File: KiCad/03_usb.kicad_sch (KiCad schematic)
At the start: 18 parts, among them IC301 CP2102N-A02-GQFN28R, J200 USB_C_Receptacle_USB2.0, J301 USB_C_Receptacle_USB2.0, U301 USBLC6-2SC6, U302 USBLC6-2SC6

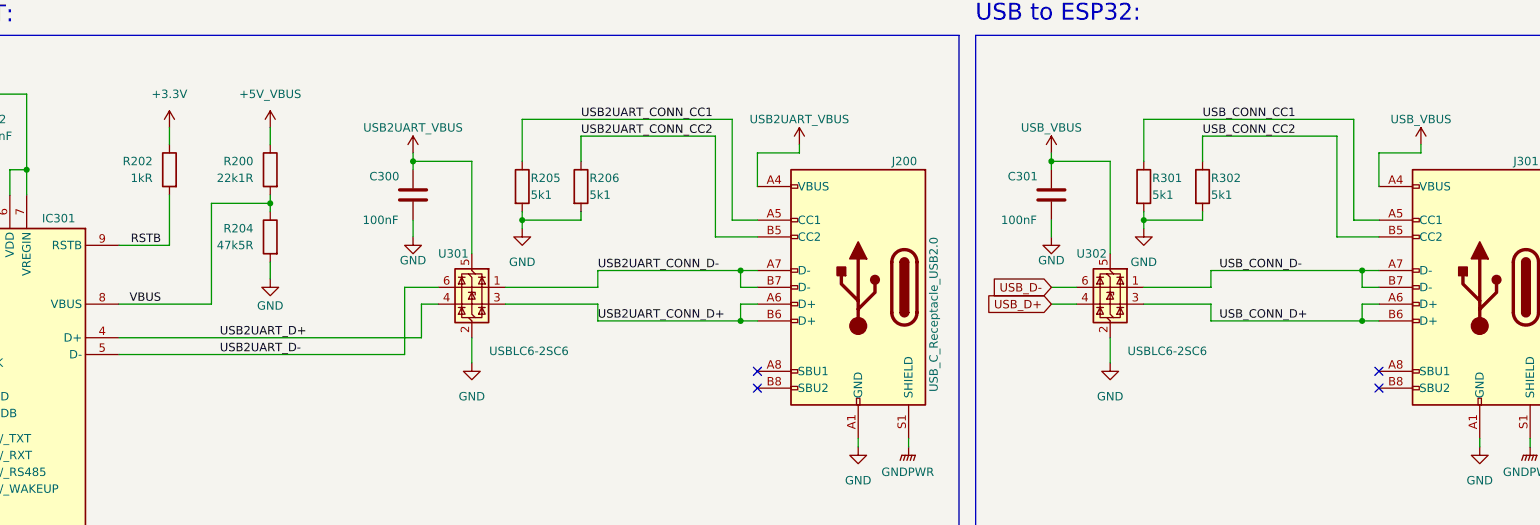
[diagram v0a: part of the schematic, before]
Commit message: Add DS3231
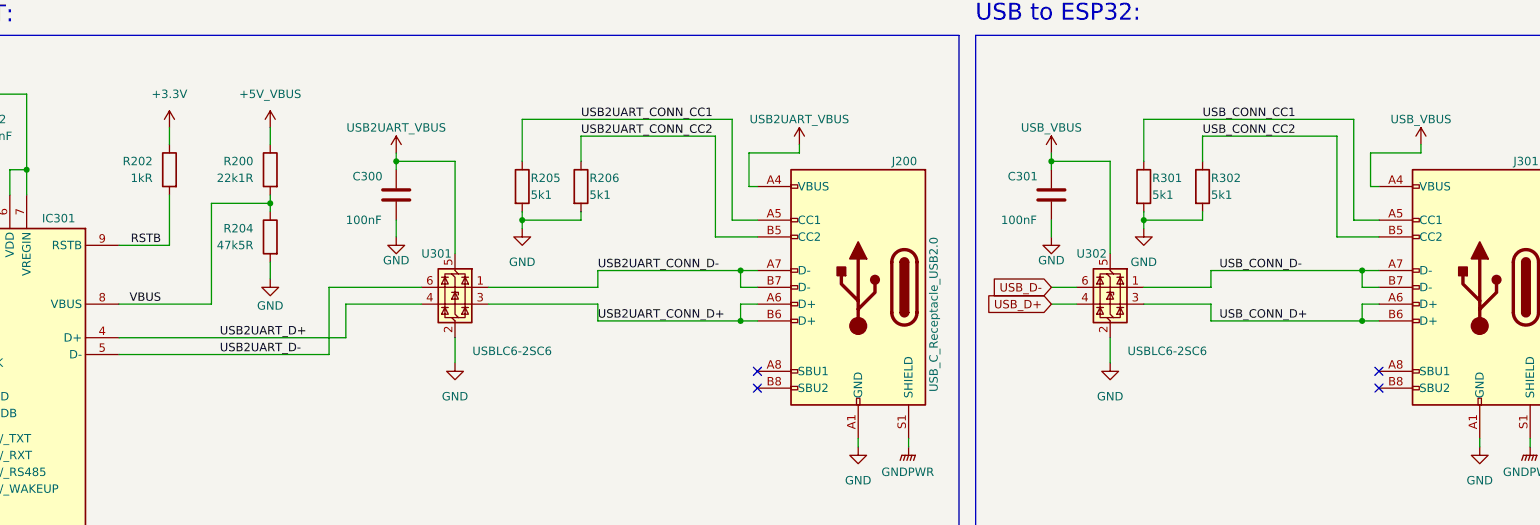
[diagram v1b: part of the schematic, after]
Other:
- moved on the sheet: C300, U301
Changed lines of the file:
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@@
 	)
 	(junction
-		(at 104.14 50.8)
+		(at 101.6 50.8)
 		(diameter 0)
 		(color 0 0 0 0)
@@
 	(wire
 		(pts
-			(xy 113.03 64.77) (xy 113.03 50.8)
+			(xy 110.49 64.77) (xy 110.49 50.8)
 		)
 		(stroke
@@
 	(wire
 		(pts
-			(xy 156.21 49.53) (xy 156.21 54.61)
+			(xy 154.94 49.53) (xy 154.94 54.61)
 		)
 		(stroke
@@
 	(wire
 		(pts
-			(xy 104.14 62.23) (xy 104.14 59.69)
+			(xy 101.6 62.23) (xy 101.6 59.69)
 		)
 		(stroke
@@
 	(wire
 		(pts
-			(xy 104.14 50.8) (xy 104.14 52.07)
+			(xy 101.6 50.8) (xy 101.6 52.07)
 		)
 		(stroke
@@
 	(wire
 		(pts
-			(xy 105.41 77.47) (xy 105.41 72.39)
+			(xy 93.98 77.47) (xy 93.98 72.39)
 		)
 		(stroke
@@
 	(wire
 		(pts
-			(xy 118.11 69.85) (xy 132.08 69.85)
+			(xy 115.57 69.85) (xy 132.08 69.85)
 		)
 		(stroke
@@
 	(wire
 		(pts
-			(xy 59.69 80.01) (xy 102.87 80.01)
+			(xy 59.69 80.01) (xy 91.44 80.01)
 		)
 		(stroke
@@
 	(wire
 		(pts
-			(xy 59.69 77.47) (xy 105.41 77.47)
+			(xy 59.69 77.47) (xy 93.98 77.47)
 		)
 		(stroke
@@
 	(wire
 		(pts
-			(xy 113.03 77.47) (xy 113.03 81.28)
+			(xy 110.49 77.47) (xy 110.49 81.28)
 		)
 		(stroke
@@
 	(wire
 		(pts
-			(xy 162.56 49.53) (xy 156.21 49.53)
+			(xy 162.56 49.53) (xy 154.94 49.53)
 		)
 		(stroke
@@
 	(wire
 		(pts
-			(xy 118.11 72.39) (xy 132.08 72.39)
+			(xy 115.57 72.39) (xy 132.08 72.39)
 		)
 		(stroke
@@
 	(wire
 		(pts
+			(xy 154.94 54.61) (xy 156.21 54.61)
+		)
+		(stroke
+			(width 0)
+			(type default)
+		)
+	)
+	(wire
+		(pts
 			(xy 224.79 72.39) (xy 224.79 74.93)
 		)
@@
 	(wire
 		(pts
-			(xy 105.41 72.39) (xy 107.95 72.39)
+			(xy 93.98 72.39) (xy 105.41 72.39)
 		)
 		(stroke
@@
 	(wire
 		(pts
-			(xy 102.87 69.85) (xy 107.95 69.85)
+			(xy 91.44 69.85) (xy 105.41 69.85)
 		)
 		(stroke
@@
 	(wire
 		(pts
-			(xy 250.19 49.53) (xy 250.19 54.61)
+			(xy 248.92 49.53) (xy 248.92 54.61)
 		)
 		(stroke
@@
 	(wire
 		(pts
-			(xy 104.14 49.53) (xy 104.14 50.8)
+			(xy 101.6 49.53) (xy 101.6 50.8)
 		)
 		(stroke
@@
 	(wire
 		(pts
+			(xy 248.92 54.61) (xy 250.19 54.61)
+		)
+		(stroke
+			(width 0)
+			(type default)
+		)
+	)
+	(wire
+		(pts
 			(xy 21.59 50.8) (xy 34.29 50.8)
 		)
@@
 	(wire
 		(pts
-			(xy 113.03 50.8) (xy 104.14 50.8)
+			(xy 110.49 50.8) (xy 101.6 50.8)
 		)
 		(stroke
@@
 	(wire
 		(pts
-			(xy 102.87 80.01) (xy 102.87 69.85)
+			(xy 91.44 80.01) (xy 91.44 69.85)
 		)
 		(stroke
@@
 	(wire
 		(pts
-			(xy 256.54 49.53) (xy 250.19 49.53)
+			(xy 256.54 49.53) (xy 248.92 49.53)
 		)
 		(stroke
@@
 	(symbol
 		(lib_id "power:VBUS")
-		(at 104.14 49.53 0)
+		(at 101.6 49.53 0)
 		(unit 1)
 		(exclude_from_sim no)
@@
 		(dnp no)
 		(property "Reference" "#PWR0311"
-			(at 104.14 53.34 0)
+			(at 101.6 53.34 0)
 			(effects
 				(font
@@
 		)
 		(property "Value" "USB2UART_VBUS"
-			(at 104.14 45.72 0)
+			(at 101.6 45.72 0)
 			(effects
 				(font
@@
 		)
 		(property "Footprint" ""
-			(at 104.14 49.53 0)
+			(at 101.6 49.53 0)
 			(effects
 				(font
@@
 		)
 		(property "Datasheet" ""
-			(at 104.14 49.53 0)
+			(at 101.6 49.53 0)
 			(effects
 				(font
@@
 		)
 		(property "Description" ""
-			(at 104.14 49.53 0)
+			(at 101.6 49.53 0)
 			(effects
 				(font
@@
 	(symbol
 		(lib_id "power:GND")
-		(at 104.14 62.23 0)
+		(at 101.6 62.23 0)
 		(mirror y)
 		(unit 1)
@@
 		(dnp no)
 		(property "Reference" "#PWR0310"
-			(at 104.14 68.58 0)
+			(at 101.6 68.58 0)
 			(effects
 				(font
@@
 		)
 		(property "Value" "GND"
-			(at 104.14 65.786 0)
+			(at 101.6 65.786 0)
 			(effects
 				(font
@@
 		)
 		(property "Footprint" ""
-			(at 104.14 62.23 0)
+			(at 101.6 62.23 0)
 			(effects
 				(font
@@
 		)
 		(property "Datasheet" ""
-			(at 104.14 62.23 0)
+			(at 101.6 62.23 0)
 			(effects
 				(font
@@
 		)
 		(property "Description" "Power symbol creates a global label with name \"GND\" , ground"
-			(at 104.14 62.23 0)
+			(at 101.6 62.23 0)
 			(effects
 				(font
@@
 	(symbol
 		(lib_id "Power_Protection:USBLC6-2SC6")
-		(at 113.03 69.85 0)
+		(at 110.49 69.85 0)
 		(mirror y)
 		(unit 1)
@@
 		(dnp no)
 		(property "Reference" "U301"
-			(at 110.236 64.77 0)
+			(at 107.696 64.77 0)
 			(effects
 				(font
@@
 		)
 		(property "Value" "USBLC6-2SC6"
-			(at 121.666 79.502 0)
+			(at 119.126 79.502 0)
 			(effects
 				(font
@@
 		)
 		(property "Footprint" "Package_TO_SOT_SMD:SOT-23-6"
-			(at 113.03 82.55 0)
+			(at 110.49 82.55 0)
 			(effects
 				(font
@@
 		)
 		(property "Datasheet" "https://www.st.com/resource/en/datasheet/usblc6-2.pdf"
-			(at 107.95 60.96 0)
+			(at 105.41 60.96 0)
 			(effects
 				(font
@@
 		)
 		(property "Description" ""
-			(at 113.03 69.85 0)
+			(at 110.49 69.85 0)
 			(effects
 				(font
@@
 		)
 		(property "Manufacturer" "STMicroelectronics"
-			(at 113.03 69.85 0)
+			(at 110.49 69.85 0)
 			(effects
 				(font
@@
 		)
 		(property "DigiKey Part Number" "497-5235-6-ND"
-			(at 113.03 69.85 0)
+			(at 110.49 69.85 0)
 			(effects
 				(font
@@
 		)
 		(property "Manufacturer Part Number" "USBLC6-2SC6"
-			(at 113.03 69.85 0)
+			(at 110.49 69.85 0)
 			(effects
 				(font
@@
 	(symbol
 		(lib_id "power:GND")
-		(at 113.03 81.28 0)
+		(at 110.49 81.28 0)
 		(unit 1)
 		(exclude_from_sim no)
@@
 		(fields_autoplaced yes)
 		(property "Reference" "#PWR026"
-			(at 113.03 87.63 0)
+			(at 110.49 87.63 0)
 			(effects
 				(font
@@
 		)
 		(property "Value" "GND"
-			(at 113.03 86.36 0)
+			(at 110.49 86.36 0)
 			(effects
 				(font
@@
 		)
 		(property "Footprint" ""
-			(at 113.03 81.28 0)
+			(at 110.49 81.28 0)
 			(effects
 				(font
@@
 		)
 		(property "Datasheet" ""
-			(at 113.03 81.28 0)
+			(at 110.49 81.28 0)
 			(effects
 				(font
@@
 		)
 		(property "Description" "Power symbol creates a global label with name \"GND\" , ground"
-			(at 113.03 81.28 0)
+			(at 110.49 81.28 0)
 			(effects
 				(font
@@
 	(symbol
 		(lib_id "Device:C")
-		(at 104.14 55.88 0)
+		(at 101.6 55.88 0)
 		(unit 1)
 		(exclude_from_sim no)
@@
 		(dnp no)
 		(property "Reference" "C300"
-			(at 97.536 53.086 0)
+			(at 94.996 53.086 0)
 			(effects
 				(font
@@
 		)
 		(property "Value" "100nF"
-			(at 96.52 59.69 0)
+			(at 93.98 59.69 0)
 			(effects
 				(font
@@
 		)
 		(property "Footprint" "Capacitor_SMD:C_0402_1005Metric"
-			(at 105.1052 59.69 0)
+			(at 102.5652 59.69 0)
 			(effects
 				(font
@@
 		)
 		(property "Datasheet" "~"
-			(at 104.14 55.88 0)
+			(at 101.6 55.88 0)
 			(effects
 				(font
@@
 		)
 		(property "Description" ""
-			(at 104.14 55.88 0)
+			(at 101.6 55.88 0)
 			(effects
 				(font
@@
 		)
 		(property "Manufacturer" "Samsung Electro-Mechanics"
-			(at 104.14 55.88 0)
+			(at 101.6 55.88 0)
 			(effects
 				(font
@@
 		)
 		(property "DigiKey Part Number" "1276-1002-6-ND"
-			(at 104.14 55.88 0)
+			(at 101.6 55.88 0)
 			(effects
 				(font
@@
 		)
 		(property "Manufacturer Part Number" "CL05B104KO5NNNC"
-			(at 104.14 55.88 90)
+			(at 101.6 55.88 90)
 			(effects
 				(font

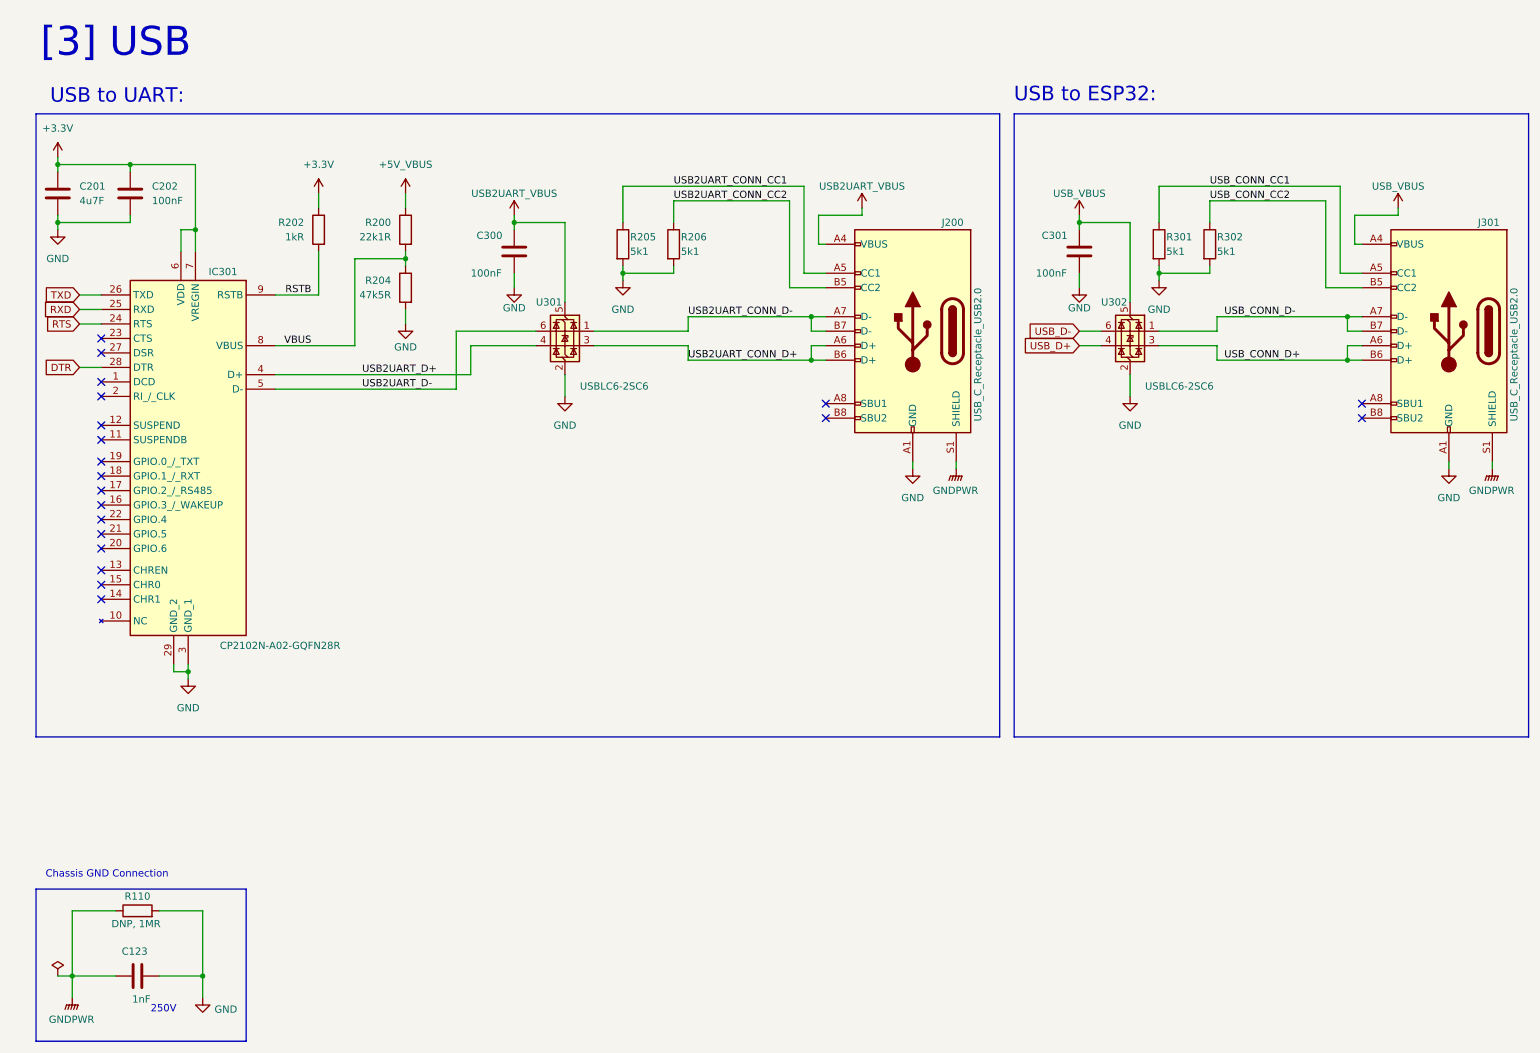
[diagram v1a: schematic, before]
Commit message: Add analog sensors
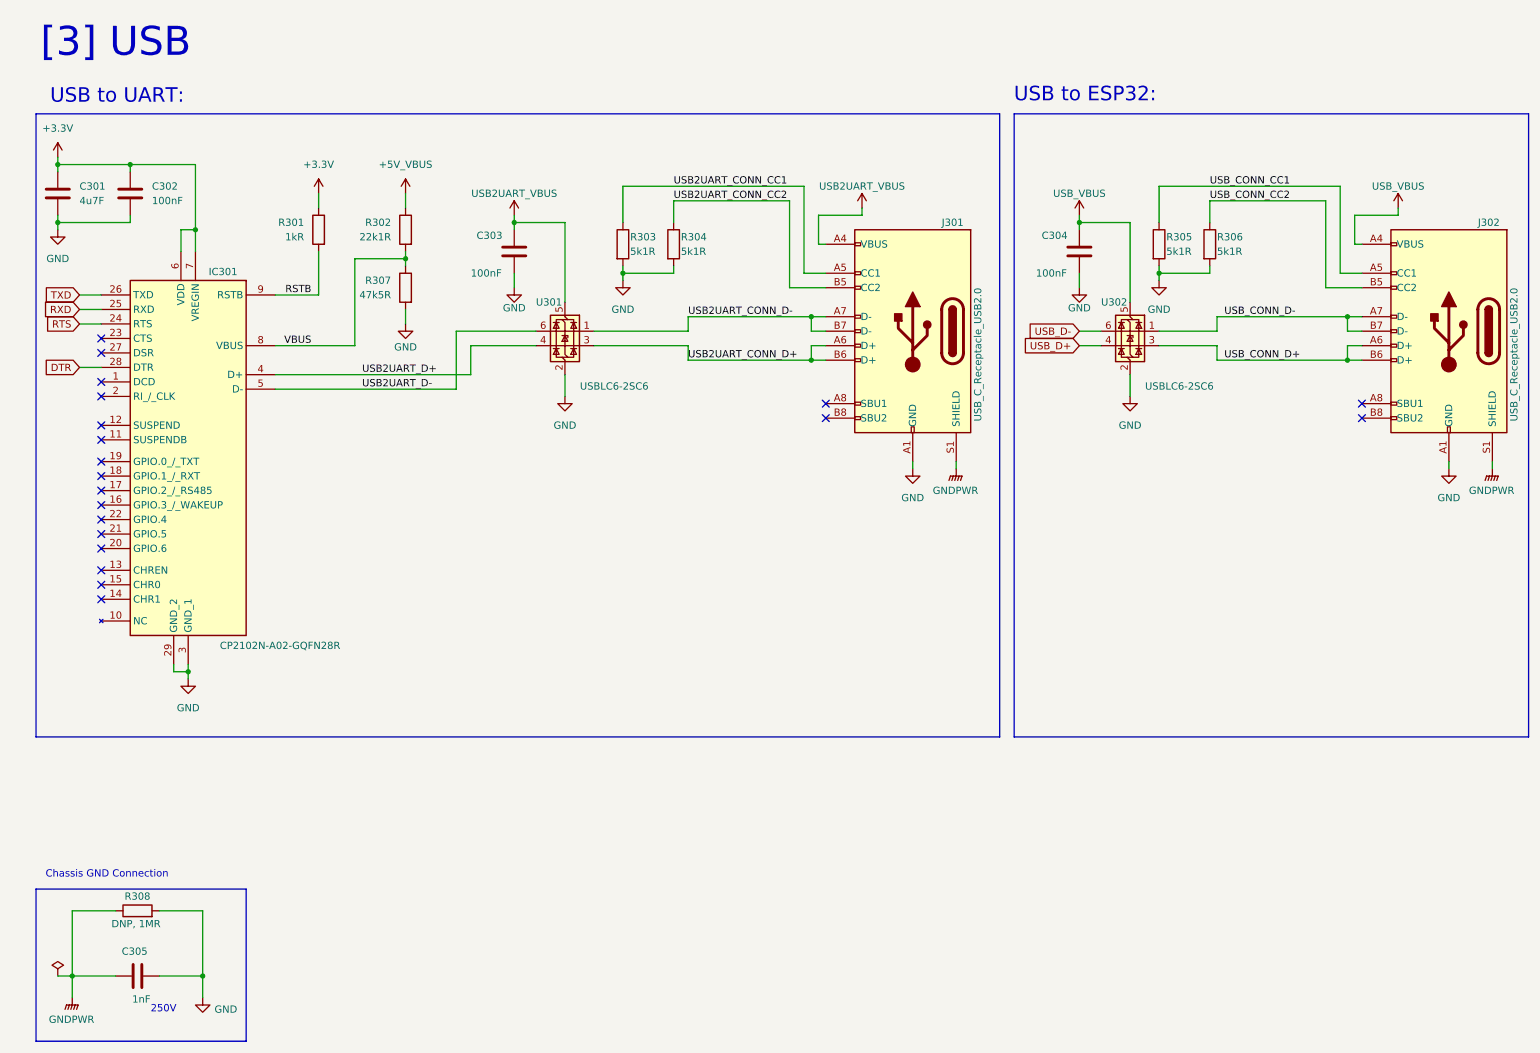
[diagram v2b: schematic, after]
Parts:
- R303: renamed from R205; value 5k1 -> 5k1R
- R304: renamed from R206; value 5k1 -> 5k1R
- R305: renamed from R301; value 5k1 -> 5k1R
- R306: renamed from R302; value 5k1 -> 5k1R
- renumbered C201 to C301, C202 to C302, C300 to C303, C301 to C304, C123 to C305, J200 to J301, J301 to J302, R202 to R301, R200 to R302, R204 to R307, R110 to R308

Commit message: First scheme version
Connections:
- net +3.3V renamed +3V3
- net +5V_VBUS renamed +VCC_USB2UART_FILT

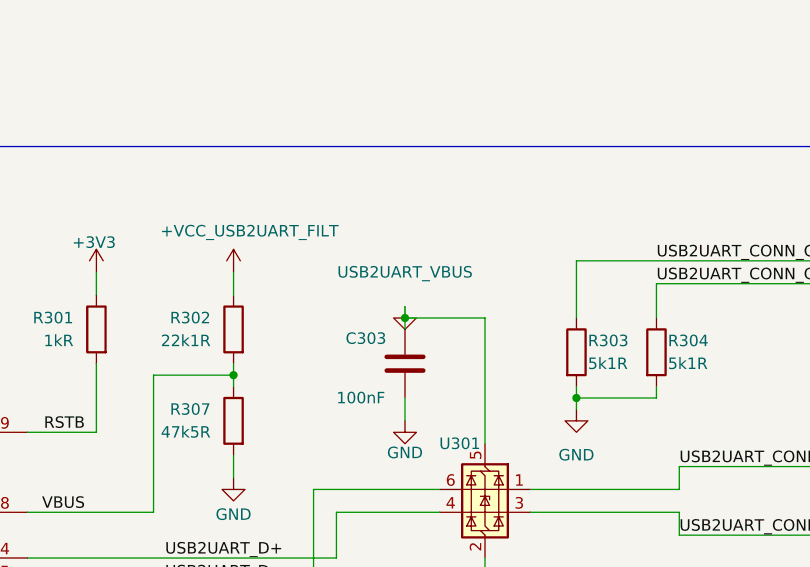
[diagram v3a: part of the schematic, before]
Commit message: Add UART pin header
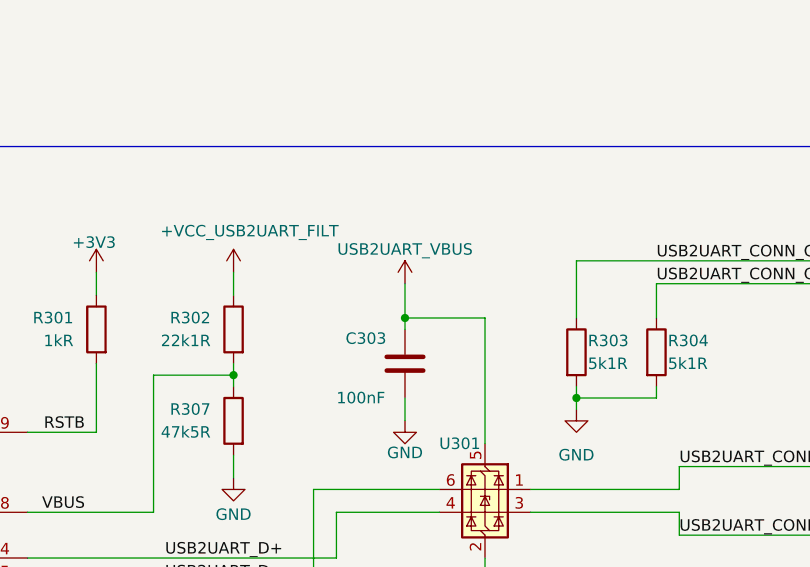
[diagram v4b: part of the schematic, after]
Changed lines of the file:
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@@
 	(wire
 		(pts
-			(xy 101.6 49.53) (xy 101.6 50.8)
+			(xy 101.6 46.99) (xy 101.6 50.8)
 		)
 		(stroke
@@
 	)
 	(symbol
-		(lib_name "GND_8")
-		(lib_id "power:GND")
-		(at 101.6 49.53 0)
-		(unit 1)
-		(exclude_from_sim no)
-		(in_bom yes)
-		(on_board yes)
-		(dnp no)
-		(property "Reference" "#PWR0306"
-			(at 101.6 53.34 0)
-			(effects
-				(font
-					(size 1.27 1.27)
-				)
-				(hide yes)
-			)
-		)
-		(property "Value" "USB2UART_VBUS"
-			(at 101.6 45.72 0)
-			(effects
-				(font
-					(size 1.27 1.27)
-				)
-			)
-		)
-		(property "Footprint" ""
-			(at 101.6 49.53 0)
-			(effects
-				(font
-					(size 1.27 1.27)
-				)
-				(hide yes)
-			)
-		)
-		(property "Datasheet" ""
-			(at 101.6 49.53 0)
-			(effects
-				(font
-					(size 1.27 1.27)
-				)
-				(hide yes)
-			)
-		)
-		(property "Description" "Power symbol creates a global label with name \"GND\" , ground"
-			(at 101.6 49.53 0)
-			(effects
-				(font
-					(size 1.27 1.27)
-				)
-				(hide yes)
-			)
-		)
-		(pin "1"
-		)
-		(instances
-			(project "esp32_s3_weather_webserver"
-				(path "/04e96486-ec4c-4881-a0bf-37cb6ce91c2d/03b8cdb9-87b3-40fb-b75a-b9ce0b7f30b6"
-					(reference "#PWR0306")
-					(unit 1)
-				)
-			)
-		)
-	)
-	(symbol
 		(lib_id "Power_Protection:USBLC6-2SC6")
 		(at 110.49 69.85 0)
@@
 					(unit 1)
 				)
+			)
+		)
+	)
+	(symbol
+		(lib_id "power:VBUS")
+		(at 101.6 46.99 0)
+		(unit 1)
+		(exclude_from_sim no)
+		(in_bom yes)
+		(on_board yes)
+		(dnp no)
+		(property "Reference" "#PWR011"
+			(at 101.6 50.8 0)
+			(effects
+				(font
+					(size 1.27 1.27)
+				)
+				(hide yes)
+			)
+		)
+		(property "Value" "USB2UART_VBUS"
+			(at 101.6 43.18 0)
+			(effects
+				(font
+					(size 1.27 1.27)
+				)
+			)
+		)
+		(property "Footprint" ""
+			(at 101.6 46.99 0)
+			(effects
+				(font
+					(size 1.27 1.27)
+				)
+				(hide yes)
+			)
+		)
+		(property "Datasheet" ""
+			(at 101.6 46.99 0)
+			(effects
+				(font
+					(size 1.27 1.27)
+				)
+				(hide yes)
+			)
+		)
+		(property "Description" "Power symbol creates a global label with name \"VBUS\""
+			(at 101.6 46.99 0)
+			(effects
+				(font
+					(size 1.27 1.27)
+				)
+				(hide yes)
+			)
+		)
+		(pin "1"
+		)
+		(instances
+			(project "esp32_s3_weather_webserver"
+				(path "/04e96486-ec4c-4881-a0bf-37cb6ce91c2d/03b8cdb9-87b3-40fb-b75a-b9ce0b7f30b6"
+					(reference "#PWR011")
+					(unit 1)
+				)
